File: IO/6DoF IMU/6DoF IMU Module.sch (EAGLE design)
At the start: 3 parts

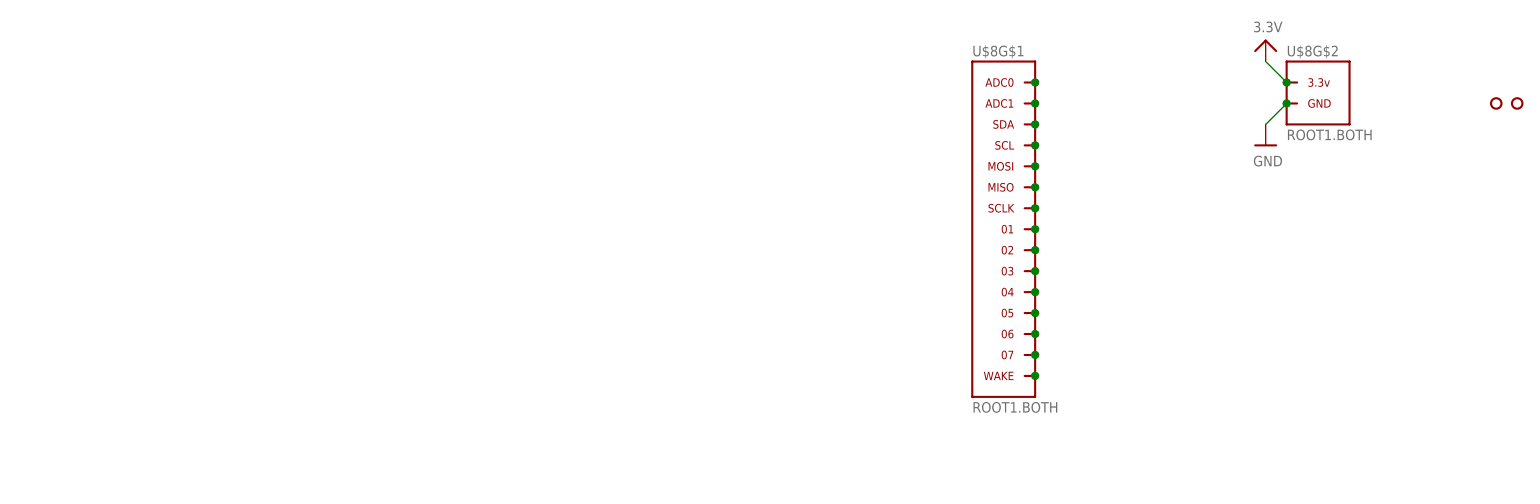
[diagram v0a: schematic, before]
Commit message: Updated concepts/ideas Renamed 6DoF IMU files Created 6DoF IMU sch and brd  (Missing 8-1 smd jumper)
Signed-off-by: Cruz Monrreal II <Cruz.Monrreal@gmail.com>
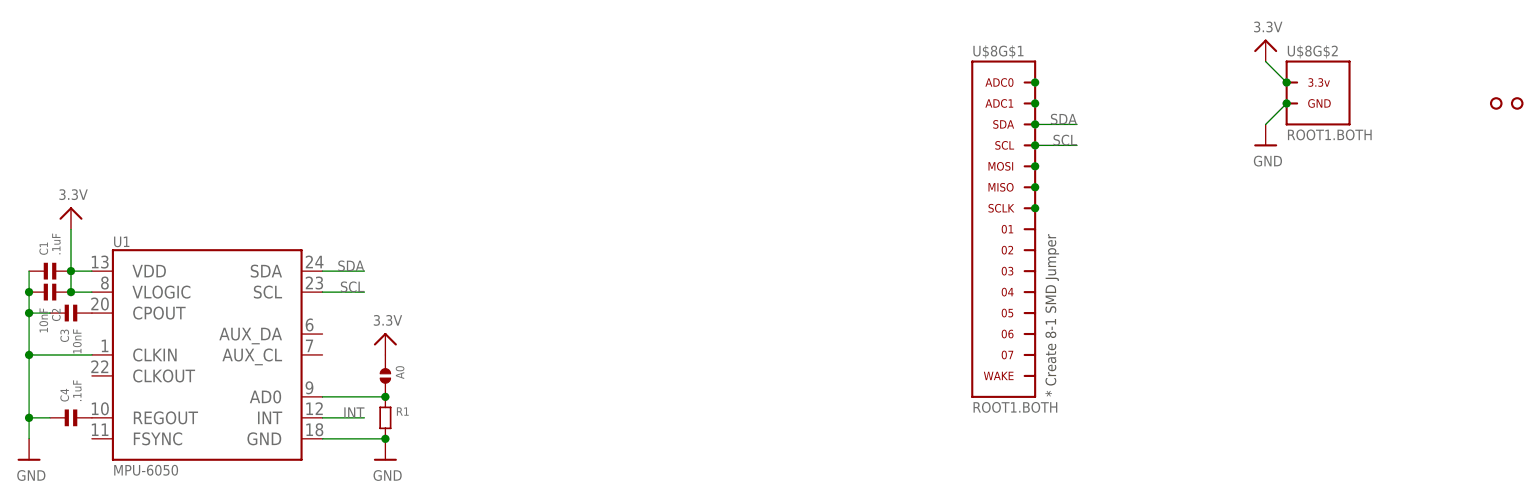
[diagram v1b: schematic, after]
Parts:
- added A0: (no value), .solderjumper:SOLDERJUMPER.2.LRG
- added C1, C4: .1uF, .standardparts:CAPACITOR.0603
- added C2, C3: 10nF, .standardparts:CAPACITOR.0603
- added R1: (no value), .standardparts:RESISTOR.0603
- added U1: MPU-6050, invensense:MPU-6050
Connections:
- removed net N$10: U$8G$1.03
- removed net N$11: U$8G$1.04
- removed net N$12: U$8G$1.05
- removed net N$13: U$8G$1.06
- removed net N$14: U$8G$1.07
- removed net N$15: U$8G$1.WAKE
- removed net N$3: U$8G$1.SDA
- removed net N$4: U$8G$1.SCL
- removed net N$8: U$8G$1.01
- removed net N$9: U$8G$1.02
- new net INT: U1.INT
- new net N$16: C3.2, U1.CPOUT
- new net N$18: A0.2, R1.1, U1.AD0
- new net N$20: C4.2, U1.REGOUT
- new net SCL: U$8G$1.SCL, U1.SCL
- new net SDA: U$8G$1.SDA, U1.SDA
- net 3.3V: now also A0.1, C1.2, C2.1, U1.VDD, U1.VLOGIC
- net GND: now also C1.1, C2.2, C3.1, C4.1, R1.2, U1.CLKIN, U1.GND
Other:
- note added: "* Create 8-1 SMD Jumper"
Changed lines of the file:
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@@
 <part name="U$3" library=".screw_holes" deviceset="HOLE" device=".2MM"/>
 <part name="U$8" library="thinkmaketest" deviceset="ROOT1" device=".BOTH"/>
+<part name="U1" library="invensense" deviceset="MPU-6050" device=""/>
+<part name="U$7" library="microbuilder" deviceset="3.3V" device=""/>
+<part name="U$9" library="microbuilder" deviceset="GND" device=""/>
+<part name="C1" library=".standardparts" deviceset="CAPACITOR" device=".0603" value=".1uF"/>
+<part name="C2" library=".standardparts" deviceset="CAPACITOR" device=".0603" value="10nF"/>
+<part name="C3" library=".standardparts" deviceset="CAPACITOR" device=".0603" value="10nF"/>
+<part name="C4" library=".standardparts" deviceset="CAPACITOR" device=".0603" value=".1uF"/>
+<part name="U$10" library="microbuilder" deviceset="GND" device=""/>
+<part name="A0" library=".solderjumper" deviceset="SOLDERJUMPER.2" device=".LRG"/>
+<part name="R1" library=".standardparts" deviceset="RESISTOR" device=".0603"/>
+<part name="U$11" library="microbuilder" deviceset="3.3V" device=""/>
 </parts>
 <sheets>
 <sheet>
 <plain>
+<text x="177.8" y="91.44" size="1.27" layer="97" rot="R90">* Create 8-1 SMD Jumper</text>
 </plain>
 <instances>
@@
 <instance part="U$8" gate="G$1" x="172.72" y="111.76"/>
 <instance part="U$8" gate="G$2" x="210.82" y="127"/>
+<instance part="U1" gate="G$1" x="73.66" y="96.52"/>
+<instance part="U$7" gate="G$1" x="58.42" y="111.76"/>
+<instance part="U$9" gate="G$1" x="96.52" y="83.82"/>
+<instance part="C1" gate="G$1" x="55.88" y="106.68"/>
+<instance part="C2" gate="G$1" x="55.88" y="104.14" rot="R180"/>
+<instance part="C3" gate="G$1" x="58.42" y="101.6" rot="MR180"/>
+<instance part="C4" gate="G$1" x="58.42" y="88.9"/>
+<instance part="U$10" gate="G$1" x="53.34" y="83.82"/>
+<instance part="A0" gate="G$1" x="96.52" y="93.98" rot="R270"/>
+<instance part="R1" gate="G$1" x="96.52" y="88.9" rot="R270"/>
+<instance part="U$11" gate="G$1" x="96.52" y="96.52"/>
 </instances>
 <busses>
@@
 <junction x="205.74" y="127"/>
 </segment>
+<segment>
+<pinref part="U1" gate="G$1" pin="GND"/>
+<pinref part="U$9" gate="G$1" pin="GND"/>
+<wire x1="88.9" y1="86.36" x2="96.52" y2="86.36" width="0.1524" layer="91"/>
+<pinref part="R1" gate="G$1" pin="2"/>
+<junction x="96.52" y="86.36"/>
+</segment>
+<segment>
+<wire x1="53.34" y1="101.6" x2="53.34" y2="96.52" width="0.1524" layer="91"/>
+<pinref part="C3" gate="G$1" pin="1"/>
+<wire x1="55.88" y1="101.6" x2="53.34" y2="101.6" width="0.1524" layer="91"/>
+<pinref part="U1" gate="G$1" pin="CLKIN"/>
+<wire x1="60.96" y1="96.52" x2="53.34" y2="96.52" width="0.1524" layer="91"/>
+<pinref part="U$10" gate="G$1" pin="GND"/>
+<wire x1="53.34" y1="86.36" x2="53.34" y2="88.9" width="0.1524" layer="91"/>
+<junction x="53.34" y="96.52"/>
+<pinref part="C1" gate="G$1" pin="1"/>
+<pinref part="C2" gate="G$1" pin="2"/>
+<wire x1="53.34" y1="88.9" x2="53.34" y2="96.52" width="0.1524" layer="91"/>
+<wire x1="53.34" y1="106.68" x2="53.34" y2="104.14" width="0.1524" layer="91"/>
+<wire x1="53.34" y1="104.14" x2="53.34" y2="101.6" width="0.1524" layer="91"/>
+<junction x="53.34" y="104.14"/>
+<junction x="53.34" y="101.6"/>
+<pinref part="C4" gate="G$1" pin="1"/>
+<wire x1="55.88" y1="88.9" x2="53.34" y2="88.9" width="0.1524" layer="91"/>
+<junction x="53.34" y="88.9"/>
+</segment>
 </net>
 <net name="3.3V" class="0">
@@
 <wire x1="205.74" y1="129.54" x2="203.2" y2="132.08" width="0.1524" layer="91"/>
 <junction x="205.74" y="129.54"/>
+</segment>
+<segment>
+<pinref part="U1" gate="G$1" pin="VLOGIC"/>
+<pinref part="U1" gate="G$1" pin="VDD"/>
+<pinref part="C1" gate="G$1" pin="2"/>
+<wire x1="58.42" y1="104.14" x2="60.96" y2="104.14" width="0.1524" layer="91"/>
+<wire x1="60.96" y1="106.68" x2="58.42" y2="106.68" width="0.1524" layer="91"/>
+<wire x1="58.42" y1="104.14" x2="58.42" y2="106.68" width="0.1524" layer="91"/>
+<junction x="58.42" y="106.68"/>
+<pinref part="U$7" gate="G$1" pin="3.3V"/>
+<wire x1="58.42" y1="111.76" x2="58.42" y2="106.68" width="0.1524" layer="91"/>
+<pinref part="C2" gate="G$1" pin="1"/>
+<junction x="58.42" y="104.14"/>
+</segment>
+<segment>
+<pinref part="A0" gate="G$1" pin="1"/>
+<pinref part="U$11" gate="G$1" pin="3.3V"/>
 </segment>
 </net>
@@
 <pinref part="U$8" gate="G$1" pin="ADC1"/>
 <junction x="175.26" y="127"/>
-</segment>
-</net>
-<net name="N$3" class="0">
-<segment>
-<pinref part="U$8" gate="G$1" pin="SDA"/>
-<junction x="175.26" y="124.46"/>
-</segment>
-</net>
-<net name="N$4" class="0">
-<segment>
-<pinref part="U$8" gate="G$1" pin="SCL"/>
-<junction x="175.26" y="121.92"/>
 </segment>
 </net>
@@
 </segment>
 </net>
-<net name="N$8" class="0">
+<net name="N$16" class="0">
 <segment>
-<pinref part="U$8" gate="G$1" pin="01"/>
-<junction x="175.26" y="111.76"/>
+<pinref part="U1" gate="G$1" pin="CPOUT"/>
+<pinref part="C3" gate="G$1" pin="2"/>
 </segment>
 </net>
-<net name="N$9" class="0">
+<net name="N$20" class="0">
 <segment>
-<pinref part="U$8" gate="G$1" pin="02"/>
-<junction x="175.26" y="109.22"/>
+<pinref part="C4" gate="G$1" pin="2"/>
+<pinref part="U1" gate="G$1" pin="REGOUT"/>
 </segment>
 </net>
-<net name="N$10" class="0">
+<net name="SDA" class="0">
 <segment>
-<pinref part="U$8" gate="G$1" pin="03"/>
-<junction x="175.26" y="106.68"/>
+<pinref part="U1" gate="G$1" pin="SDA"/>
+<wire x1="88.9" y1="106.68" x2="93.98" y2="106.68" width="0.1524" layer="91"/>
+<label x="93.98" y="106.68" size="1.27" layer="95" rot="MR0"/>
+</segment>
+<segment>
+<pinref part="U$8" gate="G$1" pin="SDA"/>
+<junction x="175.26" y="124.46"/>
+<wire x1="175.26" y1="124.46" x2="180.34" y2="124.46" width="0.1524" layer="91"/>
+<label x="180.34" y="124.46" size="1.27" layer="95" rot="MR0"/>
 </segment>
 </net>
-<net name="N$11" class="0">
+<net name="SCL" class="0">
 <segment>
-<pinref part="U$8" gate="G$1" pin="04"/>
-<junction x="175.26" y="104.14"/>
+<pinref part="U1" gate="G$1" pin="SCL"/>
+<wire x1="93.98" y1="104.14" x2="88.9" y2="104.14" width="0.1524" layer="91"/>
+<label x="93.98" y="104.14" size="1.27" layer="95" rot="MR0"/>
+</segment>
+<segment>
+<pinref part="U$8" gate="G$1" pin="SCL"/>
+<junction x="175.26" y="121.92"/>
+<wire x1="175.26" y1="121.92" x2="180.34" y2="121.92" width="0.1524" layer="91"/>
+<label x="180.34" y="121.92" size="1.27" layer="95" rot="MR0"/>
 </segment>
 </net>
-<net name="N$12" class="0">
+<net name="INT" class="0">
 <segment>
-<pinref part="U$8" gate="G$1" pin="05"/>
-<junction x="175.26" y="101.6"/>
+<pinref part="U1" gate="G$1" pin="INT"/>
+<wire x1="88.9" y1="88.9" x2="93.98" y2="88.9" width="0.1524" layer="91"/>
+<label x="93.98" y="88.9" size="1.27" layer="95" rot="MR0"/>
 </segment>
 </net>
-<net name="N$13" class="0">
+<net name="N$18" class="0">
 <segment>
-<pinref part="U$8" gate="G$1" pin="06"/>
-<junction x="175.26" y="99.06"/>
+<pinref part="R1" gate="G$1" pin="1"/>
+<pinref part="A0" gate="G$1" pin="2"/>
+<pinref part="U1" gate="G$1" pin="AD0"/>
+<wire x1="88.9" y1="91.44" x2="96.52" y2="91.44" width="0.1524" layer="91"/>
+<junction x="96.52" y="91.44"/>
 </segment>
 </net>
-<net name="N$14" class="0">
-<segment>
-<pinref part="U$8" gate="G$1" pin="07"/>
-<junction x="175.26" y="96.52"/>
-</segment>
-</net>
-<net name="N$15" class="0">
-<segment>
-<pinref part="U$8" gate="G$1" pin="WAKE"/>
-<junction x="175.26" y="93.98"/>
-</segment>
-</net>

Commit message: Renamed file to add 'Module' Schematic and Board layout complete. Needs completed Silkscreen
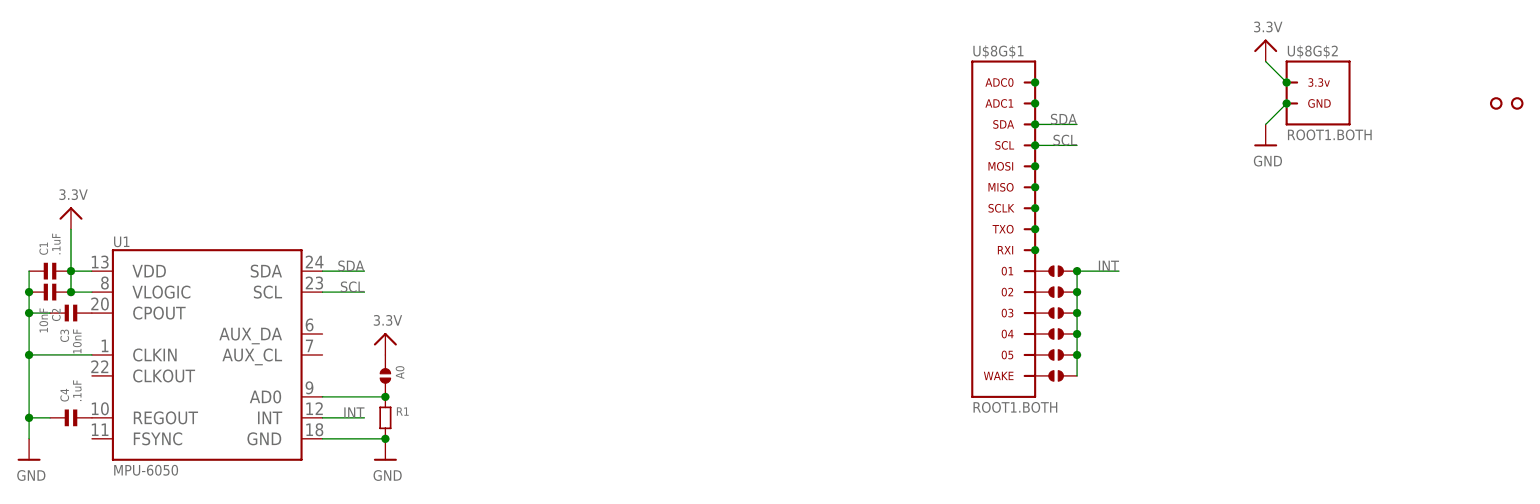
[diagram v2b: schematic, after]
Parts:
- added J1, J2, J3, J4, J5, J6: (no value), .solderjumper:SOLDERJUMPER.2.SML
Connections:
- new net N$10: J5.1, U$8G$1.05
- new net N$11: J6.1, U$8G$1.WAKE
- new net N$13: U$8G$1.RXI
- new net N$14: U$8G$1.TXO
- new net N$3: J1.1, U$8G$1.01
- new net N$4: J2.1, U$8G$1.02
- new net N$8: J3.1, U$8G$1.03
- new net N$9: J4.1, U$8G$1.04
- net INT: now also J1.2, J2.2, J3.2, J4.2, J5.2, J6.2
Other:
- note removed: "* Create 8-1 SMD Jumper"
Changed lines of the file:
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@@
 <part name="R1" library=".standardparts" deviceset="RESISTOR" device=".0603"/>
 <part name="U$11" library="microbuilder" deviceset="3.3V" device=""/>
+<part name="J1" library=".solderjumper" deviceset="SOLDERJUMPER.2" device=".SML"/>
+<part name="J2" library=".solderjumper" deviceset="SOLDERJUMPER.2" device=".SML"/>
+<part name="J3" library=".solderjumper" deviceset="SOLDERJUMPER.2" device=".SML"/>
+<part name="J4" library=".solderjumper" deviceset="SOLDERJUMPER.2" device=".SML"/>
+<part name="J5" library=".solderjumper" deviceset="SOLDERJUMPER.2" device=".SML"/>
+<part name="J6" library=".solderjumper" deviceset="SOLDERJUMPER.2" device=".SML"/>
 </parts>
 <sheets>
 <sheet>
 <plain>
-<text x="177.8" y="91.44" size="1.27" layer="97" rot="R90">* Create 8-1 SMD Jumper</text>
 </plain>
 <instances>
@@
 <instance part="R1" gate="G$1" x="96.52" y="88.9" rot="R270"/>
 <instance part="U$11" gate="G$1" x="96.52" y="96.52"/>
+<instance part="J1" gate="G$1" x="177.8" y="106.68" smashed="yes">
+<attribute name="VALUE" x="176.53" y="104.14" size="1.016" layer="96"/>
+</instance>
+<instance part="J2" gate="G$1" x="177.8" y="104.14" smashed="yes">
+<attribute name="VALUE" x="176.53" y="101.6" size="1.016" layer="96"/>
+</instance>
+<instance part="J3" gate="G$1" x="177.8" y="101.6" smashed="yes">
+<attribute name="VALUE" x="176.53" y="99.06" size="1.016" layer="96"/>
+</instance>
+<instance part="J4" gate="G$1" x="177.8" y="99.06" smashed="yes">
+<attribute name="VALUE" x="176.53" y="96.52" size="1.016" layer="96"/>
+</instance>
+<instance part="J5" gate="G$1" x="177.8" y="96.52" smashed="yes">
+<attribute name="VALUE" x="176.53" y="93.98" size="1.016" layer="96"/>
+</instance>
+<instance part="J6" gate="G$1" x="177.8" y="93.98" smashed="yes">
+<attribute name="VALUE" x="176.53" y="91.44" size="1.016" layer="96"/>
+</instance>
 </instances>
 <busses>
@@
 <label x="93.98" y="88.9" size="1.27" layer="95" rot="MR0"/>
 </segment>
+<segment>
+<pinref part="J6" gate="G$1" pin="2"/>
+<pinref part="J5" gate="G$1" pin="2"/>
+<wire x1="180.34" y1="93.98" x2="180.34" y2="96.52" width="0.1524" layer="91"/>
+<pinref part="J4" gate="G$1" pin="2"/>
+<wire x1="180.34" y1="96.52" x2="180.34" y2="99.06" width="0.1524" layer="91"/>
+<junction x="180.34" y="96.52"/>
+<pinref part="J3" gate="G$1" pin="2"/>
+<wire x1="180.34" y1="99.06" x2="180.34" y2="101.6" width="0.1524" layer="91"/>
+<junction x="180.34" y="99.06"/>
+<pinref part="J2" gate="G$1" pin="2"/>
+<wire x1="180.34" y1="101.6" x2="180.34" y2="104.14" width="0.1524" layer="91"/>
+<junction x="180.34" y="101.6"/>
+<pinref part="J1" gate="G$1" pin="2"/>
+<wire x1="180.34" y1="104.14" x2="180.34" y2="106.68" width="0.1524" layer="91"/>
+<junction x="180.34" y="104.14"/>
+<wire x1="180.34" y1="106.68" x2="185.42" y2="106.68" width="0.1524" layer="91"/>
+<junction x="180.34" y="106.68"/>
+<label x="185.42" y="106.68" size="1.27" layer="95" rot="MR0"/>
+</segment>
 </net>
 <net name="N$18" class="0">
@@
 </segment>
 </net>
+<net name="N$3" class="0">
+<segment>
+<pinref part="U$8" gate="G$1" pin="01"/>
+<pinref part="J1" gate="G$1" pin="1"/>
+</segment>
+</net>
+<net name="N$4" class="0">
+<segment>
+<pinref part="U$8" gate="G$1" pin="02"/>
+<pinref part="J2" gate="G$1" pin="1"/>
+</segment>
+</net>
+<net name="N$8" class="0">
+<segment>
+<pinref part="U$8" gate="G$1" pin="03"/>
+<pinref part="J3" gate="G$1" pin="1"/>
+</segment>
+</net>
+<net name="N$9" class="0">
+<segment>
+<pinref part="U$8" gate="G$1" pin="04"/>
+<pinref part="J4" gate="G$1" pin="1"/>
+</segment>
+</net>
+<net name="N$10" class="0">
+<segment>
+<pinref part="U$8" gate="G$1" pin="05"/>
+<pinref part="J5" gate="G$1" pin="1"/>
+</segment>
+</net>
+<net name="N$11" class="0">
+<segment>
+<pinref part="U$8" gate="G$1" pin="WAKE"/>
+<pinref part="J6" gate="G$1" pin="1"/>
+</segment>
+</net>
+<net name="N$13" class="0">
+<segment>
+<pinref part="U$8" gate="G$1" pin="RXI"/>
+<junction x="175.26" y="109.22"/>
+</segment>
+</net>
+<net name="N$14" class="0">
+<segment>
+<pinref part="U$8" gate="G$1" pin="TXO"/>
+<junction x="175.26" y="111.76"/>
+</segment>
+</net>
